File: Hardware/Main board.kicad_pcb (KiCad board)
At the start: 4 copper layers, 57.4 x 40 mm, 162 parts, among them IC1 LTC4413EDD#PBF, J1 DM3AT-SF-PEJM5_40_, J2 USB_C_Receptacle_USB2.0, J3 XT30PW-M, J4 USB_C_Receptacle_USB2.0, J5 7788, J6 7788, Q1 SISS23DN-T1-GE3, Q2 BSZ025N04LS, Q3 BSZ025N04LS, Q4 BSZ025N04LS, Q5 SSM3K15AMFV,L3F, U1 ESP32-S3, U10 TPS55288QRPMRQ1, U11 DPS368, U12 TCMT1109, U2 SN65HVD230, U3 LM66200DRLR, U4 MAX77827AEFD+T, U5 SC4215ASTRT, Y1 R940000171

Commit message: More V2 changes
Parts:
- added C19: 10uF, Capacitor_SMD:C_0402_1005Metric, B.Cu at (127.4, 87.8)
- C37: value 10uF -> 0.1uF
- R23: value 10k -> 120k
- R24: value 1.8k -> 18k
- renumbered 3V3 to 3V3LED1, PYRO_POWER to LED5
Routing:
- net /SD_CLK: track 3.59 -> 4.92 mm
- net +3V3: track 35.0 -> 35.6 mm
- net GND: vias 130 -> 169
- net Cell_Out: vias 11 -> 12
- net Cell_+: vias 28 -> 41
- added copper zone on F.Cu, net VBUS

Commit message: Board touch ups
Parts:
- renumbered LED5 to PYROPOWER

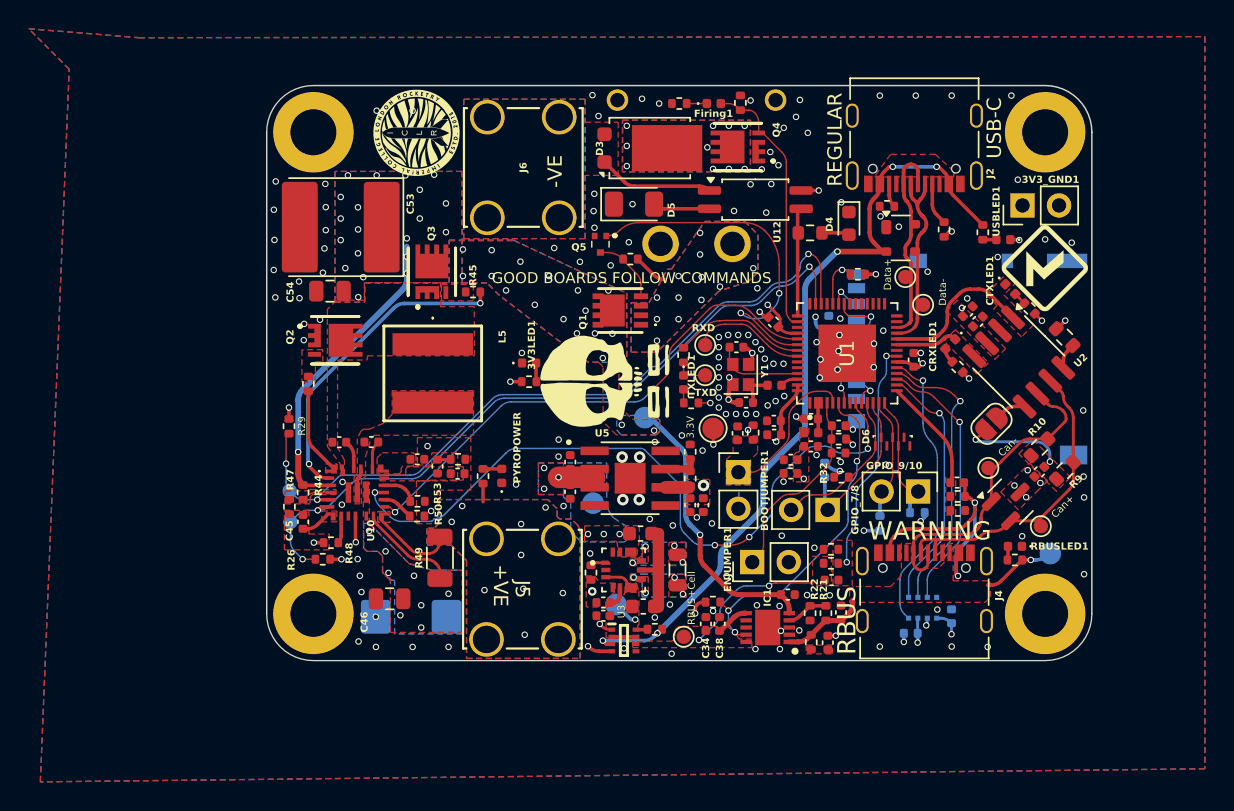
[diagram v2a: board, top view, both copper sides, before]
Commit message: More V2 changes
Mainly changed to use Ω symbol for resistors. Fixed the CDC pin for the buck boost
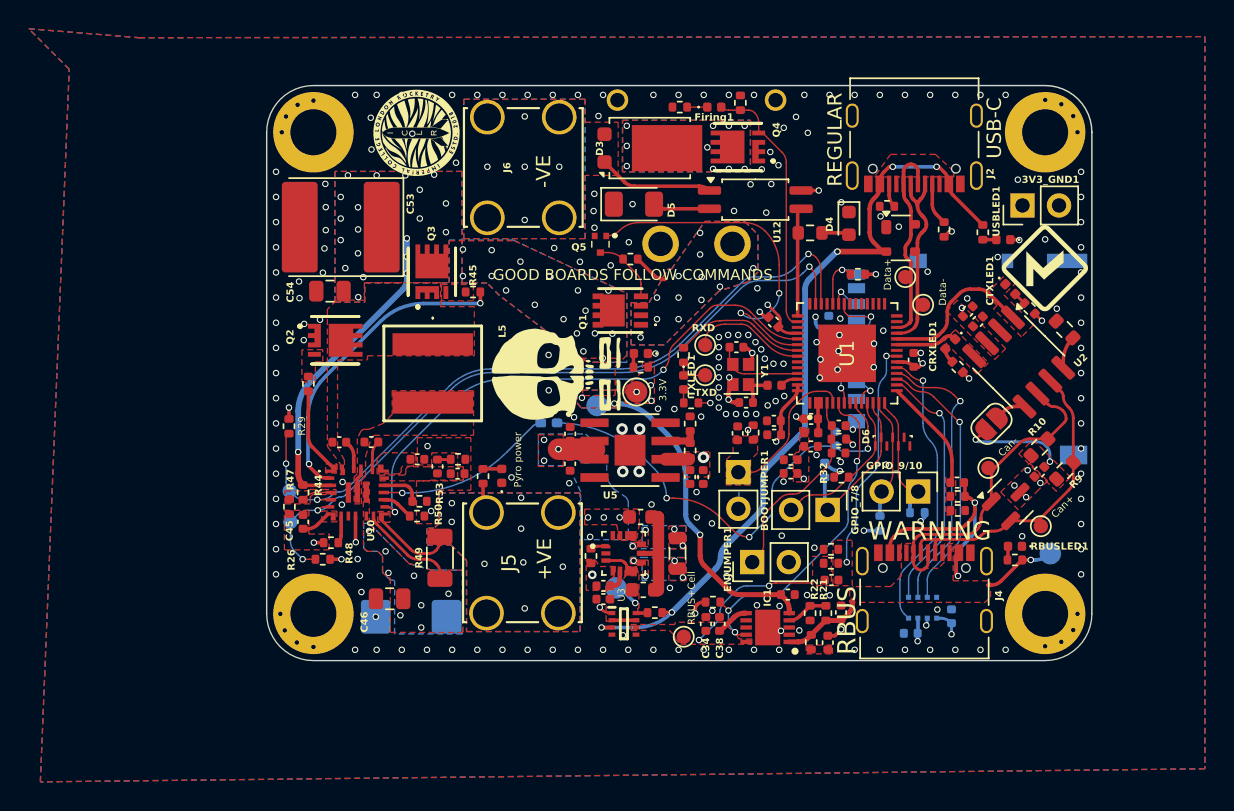
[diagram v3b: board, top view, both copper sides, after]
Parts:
- added C28: 0.1uF, Capacitor_SMD:C_0402_1005Metric, B.Cu at (127.8, 95.9)
- added JP2: CDC, Capacitor_SMD:C_0402_1005Metric_Pad0.74x0.62mm_HandSolder, B.Cu at (107.9, 94.8)
- R1, R3: value 10K -> 10kΩ
- R10, R9: value 60 -> 60Ω
- R11, R12, R13, R25: value 5.1k -> 5.1kΩ
- R14, R17, R26, R29, R35, R39, R40: value 10k -> 10kΩ
- R15: value 14k -> 14kΩ
- R16, R53: value 56k -> 56kΩ
- R18, R5: value 1k -> 1kΩ
- R19, R20: value 120 -> 120Ω
- R2, R4: value 470 -> 470Ω
- R21, R36, R47: value 100k -> 100kΩ
- R22: value 32k -> 32kΩ
- R23: value 120k -> 120kΩ
- R24, R41: value 18k -> 18kΩ
- R27: value 470k -> 470kΩ
- R37: value 1R -> 1Ω
- R44: value 178k -> 178kΩ
- R45, R46: value 10 -> 10Ω
- R48: value 49.9k -> 49.9kΩ
- R49: value 10m -> 10mΩ
- R50: value 6.19k -> 6.19kΩ
- R52: value 160k -> 160kΩ
- R7: value 3k -> 3kΩ
- R8: value 0 -> 0Ω
- moved R4 7.84 mm to (114.3, 90.9), turned to 0 degrees
- moved 3V3LED1 7.81 mm to (114.3, 90.0), turned to 180 degrees
- moved TP6 5.90 mm to (114.0, 92.7)
- moved TP8 3.53 mm to (110.5, 96.9)
- moved TP14 3.42 mm to (111.3, 93.6)
- moved G*** 3.42 mm to (108.4, 91.5)
- moved C27 1.96 mm to (118.6, 98.6)
- moved C24 1.96 mm to (109.4, 95.6)
- moved C25 1.96 mm to (109.4, 97.6)
- moved C26 1.96 mm to (117.7, 98.6)
- moved R16 1.96 mm to (117.7, 96.7)
- moved R17 1.96 mm to (117.7, 94.9)
- moved U5 1.96 mm to (113.5, 96.7)
- moved J5 1.83 mm to (103.6, 108.0)
- moved C21 1.16 mm to (114.5, 106.4)
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- renumbered PYROPOWER to LED5
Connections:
- U10 pad 16: /Current_sens -> /Voltage Regulation/CDC
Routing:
- net GND: track 30.7 -> 197.6 mm, vias 169 -> 239
- net /Current_sens: track 49.8 -> 32.0 mm, vias 4 -> 3
- net /Voltage Regulation/CDC: track 0.00 -> 12.4 mm, vias 0 -> 1
- net Cell_+: track 41.6 -> 44.2 mm
- net +3V3: track 35.6 -> 32.9 mm, vias 24 -> 25
- net /BuckBoost_INT: track 36.4 -> 38.6 mm
- net /SCL_I2C: track 52.3 -> 51.7 mm
- net /PyroPWR: vias 9 -> 8
- net /Pyro/PYRO-ve: vias 0 -> 5

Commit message: Post second Jack review
Adopted most changes
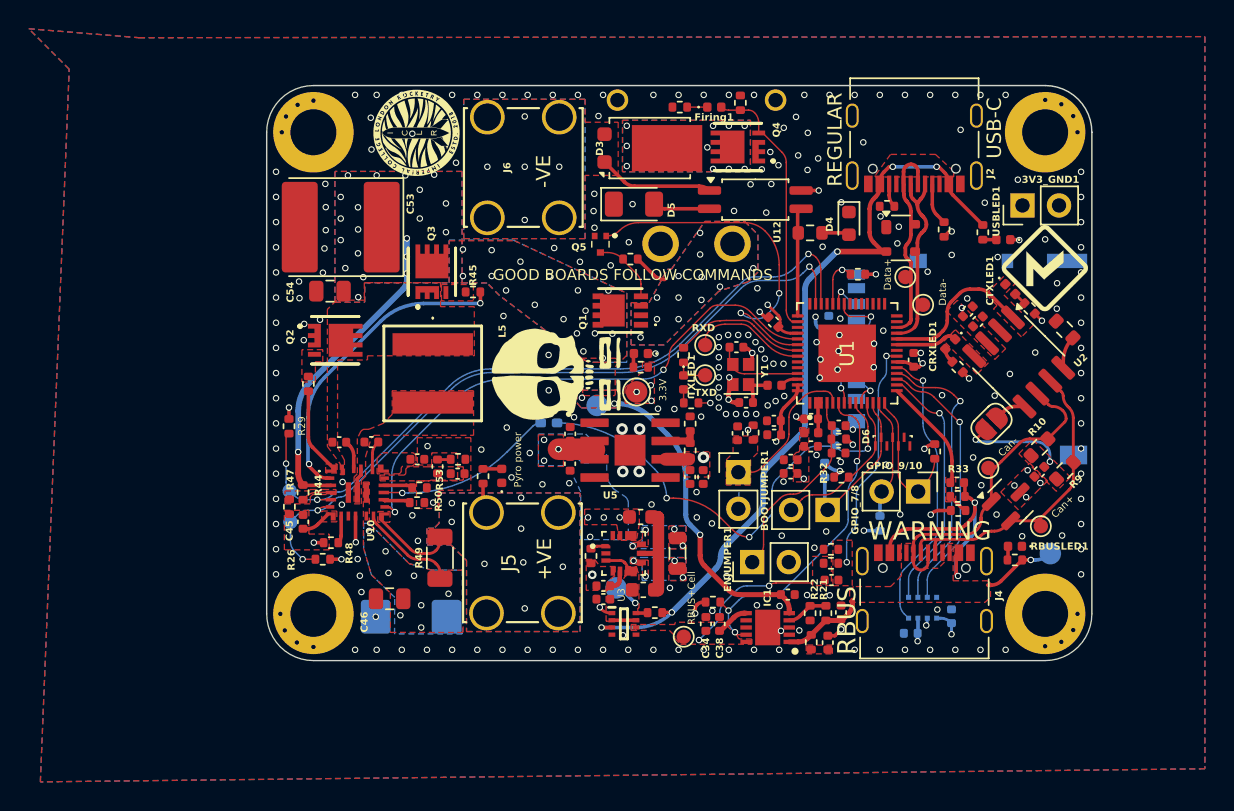
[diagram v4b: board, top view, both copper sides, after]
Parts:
- R33: moved to F.Cu
- moved R33 4.43 mm to (134.7, 96.8), turned to -90 degrees
- moved R50 0.94 mm to (98.7, 100.3)
- moved R53 0.94 mm to (98.9, 99.3)
- turned R24 to 180 degrees
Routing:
- net GND: track 197.6 -> 199.8 mm, vias 239 -> 267
- net /DeployV_LOG: track 7.85 -> 9.31 mm
- net /GPIO10: track 8.99 -> 9.96 mm
- net Net-(U10-ILIM): track 2.83 -> 2.02 mm
